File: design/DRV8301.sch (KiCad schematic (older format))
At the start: 38 parts, among them U2 LM3671, U3 DRV8301

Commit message: initial commit
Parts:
- D4: footprint Diodes_SMD:D_SMA_Handsoldering -> CRF1:SOD-123F-2
- R16, R18, R20, R22: value 2K2 -> 2k2
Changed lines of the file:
@@
 F 0 "D4" H 6800 2780 50  0000 L CNN
 F 1 "DIODE" H 6750 2620 50  0000 L CNN
-F 2 "Diodes_SMD:D_SMA_Handsoldering" V 6850 2700 50  0001 C CNN
+F 2 "CRF1:SOD-123F-2" V 6850 2700 50  0001 C CNN
 F 3 "" V 6850 2700 50  0001 C CNN
 	1    6850 2700
@@
 P 9225 4050
 F 0 "R16" V 9275 3800 50  0000 C CNN
-F 1 "2K2" V 9225 4050 50  0000 C CNN
+F 1 "2k2" V 9225 4050 50  0000 C CNN
 F 2 "Resistors_SMD:R_0603" H 9225 4050 60  0001 C CNN
 F 3 "" H 9225 4050 60  0001 C CNN
@@
 P 9225 4575
 F 0 "R18" V 9275 4325 50  0000 C CNN
-F 1 "2K2" V 9225 4575 50  0000 C CNN
+F 1 "2k2" V 9225 4575 50  0000 C CNN
 F 2 "Resistors_SMD:R_0603" H 9225 4575 60  0001 C CNN
 F 3 "" H 9225 4575 60  0001 C CNN
@@
 P 9225 5100
 F 0 "R20" V 9275 4850 50  0000 C CNN
-F 1 "2K2" V 9225 5100 50  0000 C CNN
+F 1 "2k2" V 9225 5100 50  0000 C CNN
 F 2 "Resistors_SMD:R_0603" H 9225 5100 60  0001 C CNN
 F 3 "" H 9225 5100 60  0001 C CNN
@@
 P 9225 5625
 F 0 "R22" V 9275 5375 50  0000 C CNN
-F 1 "2K2" V 9225 5625 50  0000 C CNN
+F 1 "2k2" V 9225 5625 50  0000 C CNN
 F 2 "Resistors_SMD:R_0603" H 9225 5625 60  0001 C CNN
 F 3 "" H 9225 5625 60  0001 C CNN

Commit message: initial commit
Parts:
- D4: footprint CRF1:SOD-123F-2 -> Diodes_SMD:D_SMB
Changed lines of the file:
@@
 F 0 "D4" H 6800 2780 50  0000 L CNN
 F 1 "DIODE" H 6750 2620 50  0000 L CNN
-F 2 "CRF1:SOD-123F-2" V 6850 2700 50  0001 C CNN
+F 2 "Diodes_SMD:D_SMB" V 6850 2700 50  0001 C CNN
 F 3 "" V 6850 2700 50  0001 C CNN
 	1    6850 2700

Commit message: TESC 1.4
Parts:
- U3: manf# (none) -> DRV8301DCA
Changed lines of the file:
@@
 F 2 "CRF1:TSSOP-56-PP" H 5025 3375 60  0001 C CNN
 F 3 "" H 5025 3375 60  0000 C CNN
+F 4 "DRV8301DCA" H 5025 3375 60  0001 C CNN "manf#"
 	1    5025 3375
 	1    0    0    -1

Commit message: Add manf# field
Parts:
- C13, C14, C15, C17, C20, C31, C64: manf# (none) -> C1608X5R1C225K080AB
- C16: manf# (none) -> GCD188R71H682KA01D
- C18: manf# (none) -> GRM1885C1H121JA01D
- C19: manf# (none) -> GCM188R71H223KA37J
- C21, C32: manf# (none) -> TLJA107M006R0500
- C22: manf# (none) -> GCM188R71H153KA37D
- C23, C24, C25: manf# (none) -> GCM188R71E224KA55D
- C26, C27: manf# (none) -> CGA6M3X7S2A475K200AE
- C28: manf# (none) -> C0603X104J5RACTU
- D4: manf# (none) -> NTS260ESFT3G
- D5: manf# (none) -> SMAJ5.0A
- L1: manf# (none) -> 74479275222
- L2: manf# (none) -> XAL5050-223ME
- R10: manf# (none) -> CR0603-FX-3301ELF
- R11: manf# (none) -> CRCW060318K0FKEA
- R12: manf# (none) -> CRCW060315K0FKEB
- R13: manf# (none) -> CR0603-FX-1002ELF
- R14: manf# (none) -> ERJ-3EKF2203V
- R15, R16, R17, R18, R19, R20, R21, R22: manf# (none) -> CR0603-FX-3902ELF
- U2: manf# (none) -> LM3671MF-3.3/NOPB

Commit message: Support KiCad 5.1.4
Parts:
- C13, C14, C15, C16, C17, C18, C19, C20, C22, C23, C24, C25, C28, C31, C64: footprint Capacitors_SMD:C_0603 -> Capacitor_SMD:C_0603_1608Metric; symbol C -> Device:C
- C21, C32: footprint Capacitors_Tantalum_SMD:CP_Tantalum_Case-A_EIA-3216-18_Reflow -> Capacitor_Tantalum_SMD:CP_EIA-3216-18_Kemet-A; symbol CP -> Device:CP
- C26, C27: footprint Capacitors_SMD:C_1210 -> Capacitor_SMD:C_1210_3225Metric; symbol C -> Device:C
- D4: footprint Diodes_SMD:D_SMB -> Diode_SMD:D_SMB; symbol D_Schottky_Small -> Device:D_Schottky_Small
- D5: footprint Diodes_SMD:D_SMA -> Diode_SMD:D_SMA; symbol D -> Device:D
- L1: footprint Inductors_SMD:L_0805 -> Inductor_SMD:L_0805_2012Metric; symbol L -> Device:L
- L2: symbol L -> Device:L
- R10, R11, R12, R13, R14, R15, R16, R17, R18, R19, R20, R21, R22: footprint Resistors_SMD:R_0603 -> Resistor_SMD:R_0603_1608Metric; symbol R -> Device:R
- U2: footprint TO_SOT_Packages_SMD:SOT-23-5 -> Package_TO_SOT_SMD:SOT-23-5; symbol LM3671 -> crf_1:LM3671
- U3: symbol DRV8301 -> crf_1:DRV8301
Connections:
- wire segments 137 -> 174

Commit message: Load KiCad 4.0.7 schematic symbols, footprints & 3D models
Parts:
- C13, C14, C15, C16, C17, C18, C19, C20, C22, C23, C24, C25, C28, C31, C64: footprint Capacitor_SMD:C_0603_1608Metric -> Capacitors_SMD:C_0603
- C21, C32: footprint Capacitor_Tantalum_SMD:CP_EIA-3216-18_Kemet-A -> Capacitors_Tantalum_SMD:CP_Tantalum_Case-A_EIA-3216-18_Reflow
- C26, C27: footprint Capacitor_SMD:C_1210_3225Metric -> Capacitors_SMD:C_1210
- D4: footprint Diode_SMD:D_SMB -> Diodes_SMD:D_SMB
- D5: footprint Diode_SMD:D_SMA -> Diodes_SMD:D_SMA
- L1: footprint Inductor_SMD:L_0805_2012Metric -> Inductors_SMD:L_0805
- R10, R11, R12, R13, R14, R15, R16, R17, R18, R19, R20, R21, R22: footprint Resistor_SMD:R_0603_1608Metric -> Resistors_SMD:R_0603
- U2: footprint Package_TO_SOT_SMD:SOT-23-5 -> TO_SOT_Packages_SMD:SOT-23-5

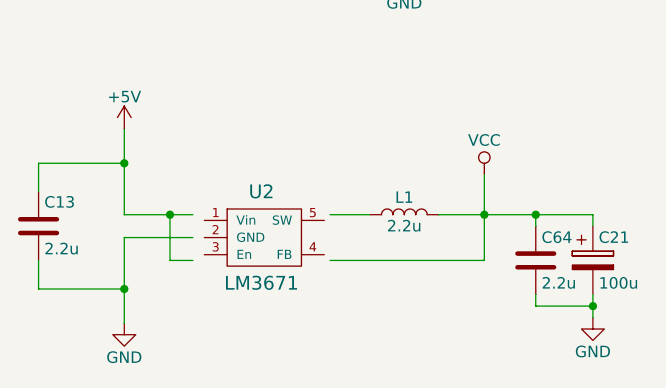
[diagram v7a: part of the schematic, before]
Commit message: Add ICM-20948 support
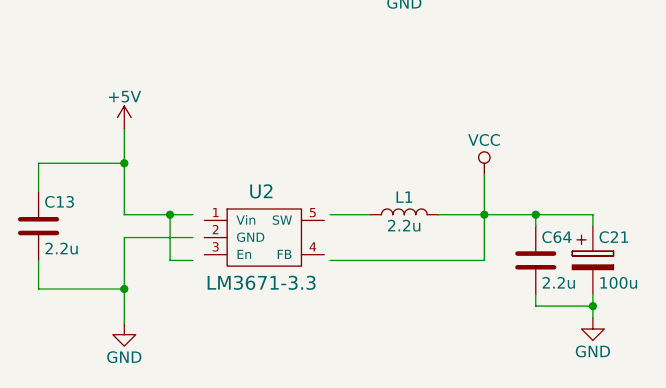
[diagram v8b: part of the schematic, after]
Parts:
- U2: value LM3671 -> LM3671-3.3
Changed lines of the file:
@@
 P 3300 6475
 F 0 "U2" H 3300 6675 60  0000 C CNN
-F 1 "LM3671" H 3300 6275 60  0000 C CNN
+F 1 "LM3671-3.3" H 3300 6275 60  0000 C CNN
 F 2 "TO_SOT_Packages_SMD:SOT-23-5" H 3250 6450 60  0001 C CNN
 F 3 "" H 3250 6450 60  0001 C CNN
